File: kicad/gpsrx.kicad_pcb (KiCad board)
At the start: 6 copper layers, 203.2 x 152.4 mm, 284 parts, among them J1 Conn_Coaxial, J10 AVR-JTAG-10, J11 JAE_SIM_Card_SF72S006, J12 Conn_Coaxial, J13 Conn_01x06, J14 Conn_01x06, J2 Conn_Coaxial, J3 Conn_Coaxial, J4 Conn_Coaxial, J5 Conn_Coaxial_Power, J6 Screw_Terminal_01x02, J7 Conn_Coaxial, J8 USB_C_Receptacle_USB2.0_14P, J9 Conn_01x03, Q1 2N7002, SW1 SW_Push, SW2 SW_Push, U1 SIT5156A, U10 AD8350ARZ20-REEL7, U11 ADP7118ACPZN, U12 ESP32-S3-WROOM-1-N8R2, U13 T20Q100F3C3, U14 TMP117xxDRV, U15 OPA376xxDBV, U16 AD5689RxRUZ, U17 JTP32CSV, U18 74AUC1G79, U19 74AUC1G79, U2 5M160ZE64, U20 PE43711B-Z, U21 LTC2386CUH-16-PBF, U22 ADP7118ACPZN, U23 LTM8074EY-PBF, U24 MONARCH_2_GM02S, U25 MCP23S17_SS, U26 TXB0108DQSR, U3 LMK1C1104, U4 LEA-M8T, U5 TDC7200, U6 LMK1C1104, U7 LTM8078EY-PBF, U8 ADP7118ACPZN, U9 ADP7118ACPZN

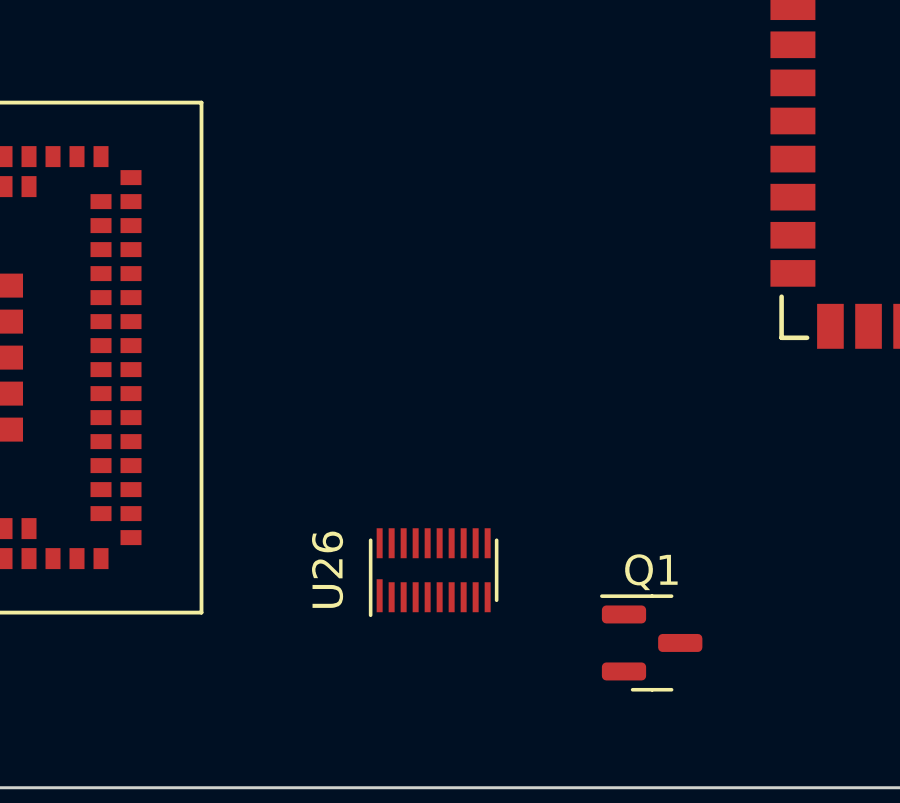
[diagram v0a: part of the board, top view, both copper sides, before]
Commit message: swap txb0108 package, fix pin 65 on cpld
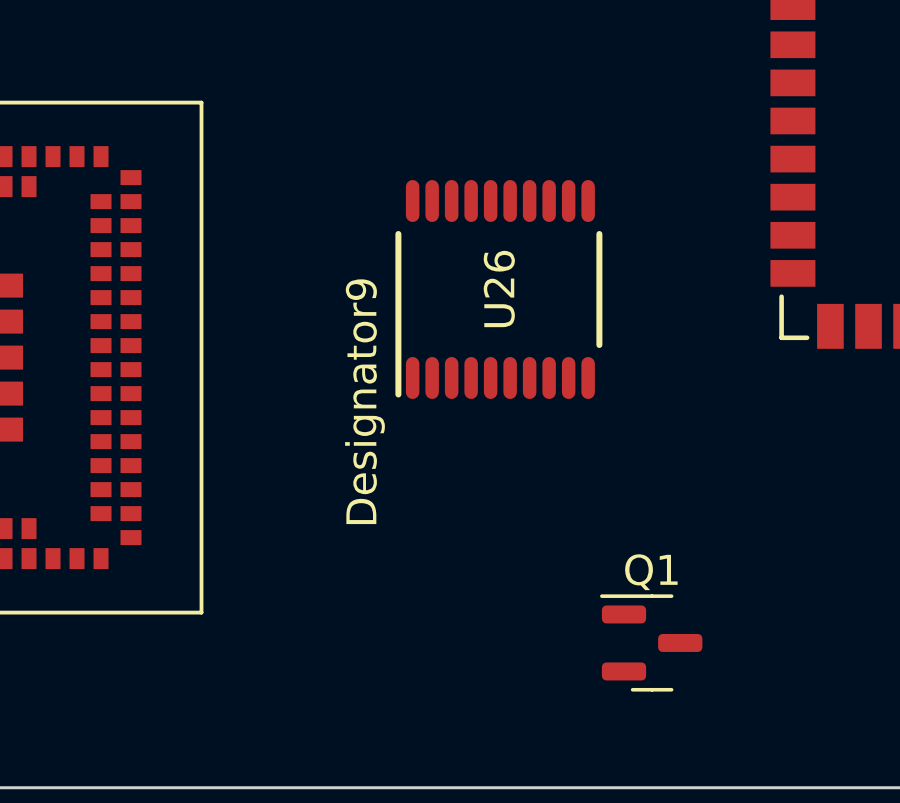
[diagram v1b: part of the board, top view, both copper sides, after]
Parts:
- U26: value TXB0108DQSR -> TXB0108PWR; footprint Package_SON:USON-20_2x4mm_P0.4mm -> bgelb_footprint:PW0020A_N
- moved U26 9.62 mm to (279.8, 190.7)
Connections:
- U26 pad 10: unconnected-(U26-A8-Pad10) -> Net-(U26-OE)
- U26 pad 11: unconnected-(U26-B8-Pad11) -> GND
- U26 pad 14: LTE_TO_UC_CTS -> unconnected-(U26-B6-Pad14)
- U26 pad 15: GND -> LTE_TO_UC_CTS
- U26 pad 16: +3.3V -> UC_TO_LTE_DATA
- U26 pad 17: UC_TO_LTE_DATA -> LTE_TO_UC_DATA
- U26 pad 18: LTE_TO_UC_DATA -> UC_TO_LTE_RTS
- U26 pad 19: UC_TO_LTE_RTS -> +3.3V
- U26 pad 2: /LTE Radio/LTE_RTS0_1V8 -> +3.3V
- U26 pad 3: /LTE Radio/LTE_TXD0_1V8 -> /LTE Radio/LTE_RTS0_1V8
- U26 pad 4: /LTE Radio/LTE_RXD0_1V8 -> /LTE Radio/LTE_TXD0_1V8
- U26 pad 5: +3.3V -> /LTE Radio/LTE_RXD0_1V8
- U26 pad 6: Net-(U26-OE) -> /LTE Radio/LTE_CTS0_1V8
- U26 pad 7: /LTE Radio/LTE_CTS0_1V8 -> unconnected-(U26-A6-Pad7)

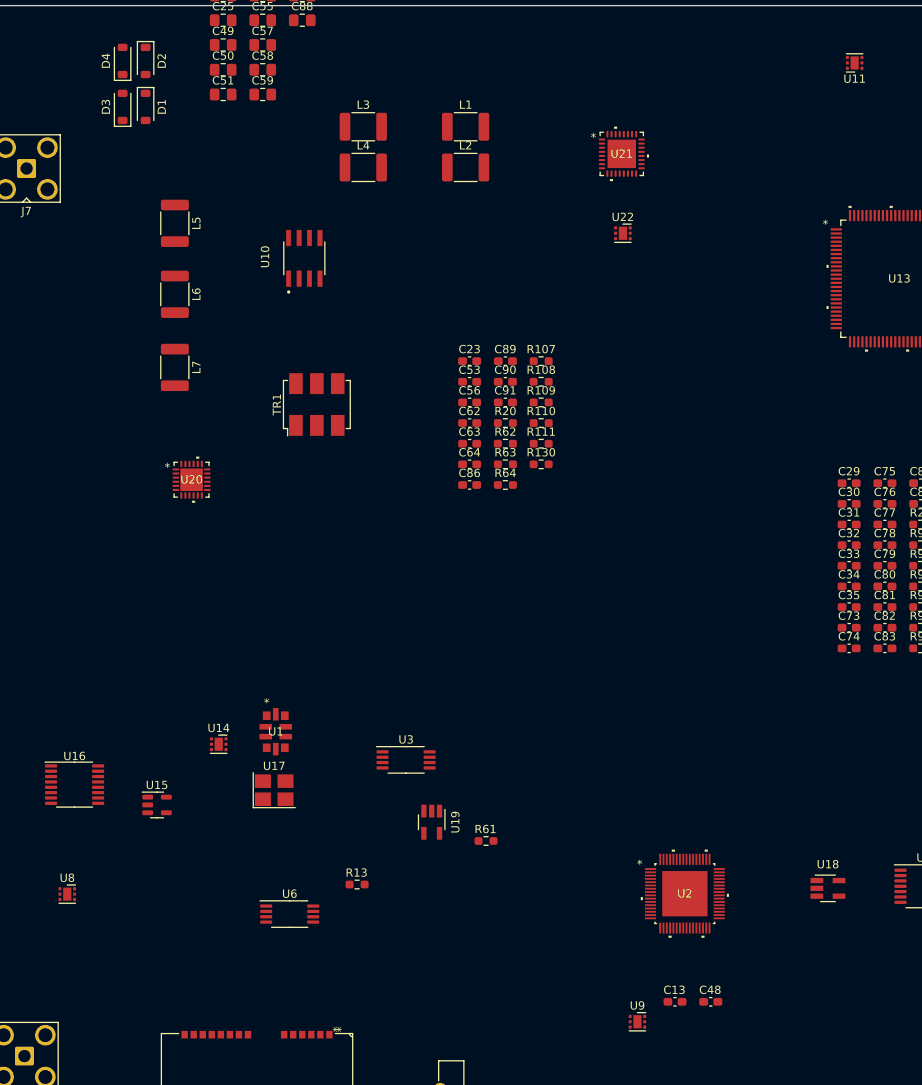
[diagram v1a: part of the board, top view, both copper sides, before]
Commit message: fix adc_clk, adp7118
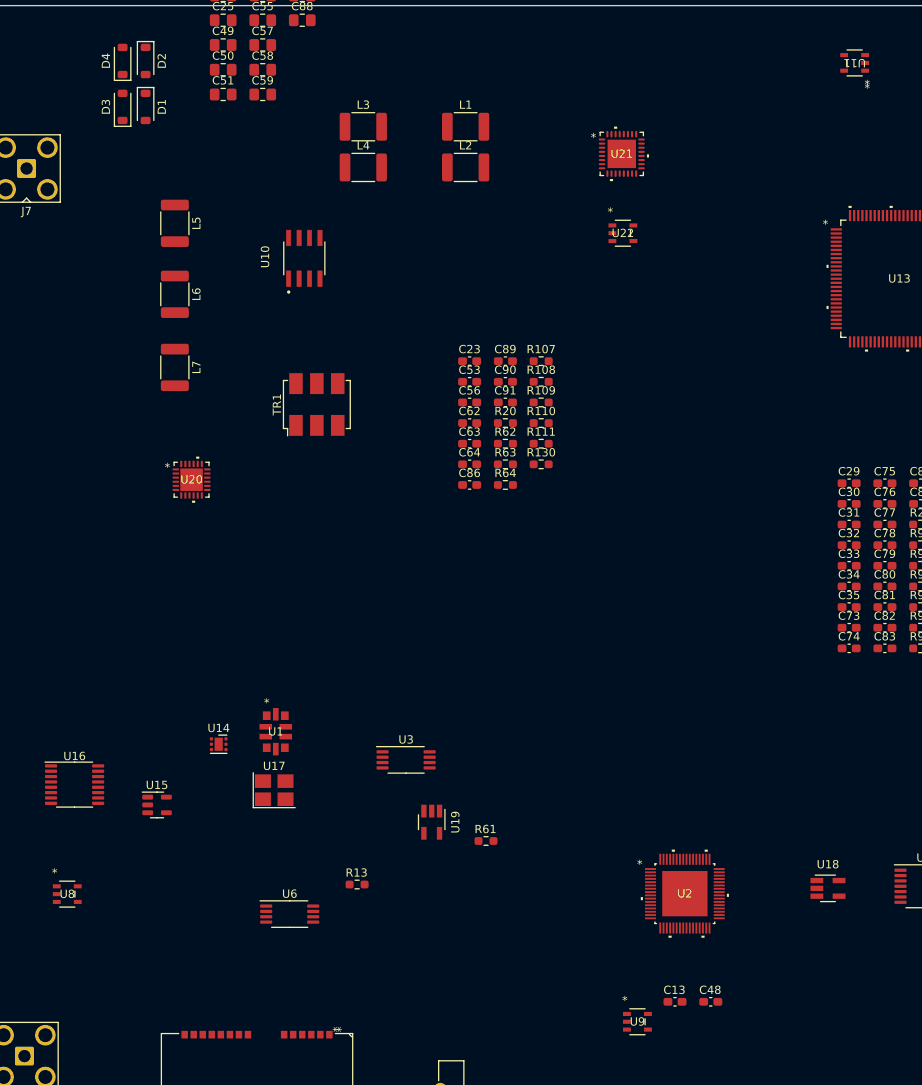
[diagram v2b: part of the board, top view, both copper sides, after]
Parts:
- U11, U22, U8, U9: value ADP7118ACPZN -> ADP7118AUJZ; footprint Package_CSP:LFCSP-6-1EP_2x2mm_P0.65mm_EP1x1.6mm -> bgelb_footprint:UJ_5_ADI
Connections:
- U11 pad 1: +2V5 -> +3.3V
- U11 pad 2: /Power/2V5_SNS -> GND
- U11 pad 3: GND -> /Power/2V5EN
- U11 pad 4: /Power/2V5EN -> /Power/2V5_SNS
- U11 pad 5: unconnected-(U11-SS-Pad5) -> +2V5
- U22 pad 1: +5VA -> /Power/5V5_OUT
- U22 pad 2: /Power/5VA_SNS -> GND
- U22 pad 3: GND -> /Power/5VA_EN
- U22 pad 4: /Power/5VA_EN -> /Power/5VA_SNS
- U22 pad 5: unconnected-(U22-SS-Pad5) -> +5VA
- U8 pad 1: +3.3VA -> /Power/5V5_OUT
- U8 pad 2: /Power/3V3A_SNS -> GND
- U8 pad 3: GND -> /Power/3V3A_EN
- U8 pad 4: /Power/3V3A_EN -> /Power/3V3A_SNS
- U8 pad 5: unconnected-(U8-SS-Pad5) -> +3.3VA
- U9 pad 1: +1V8 -> +3.3V
- U9 pad 2: /Power/1V8_SNS -> GND
- U9 pad 3: GND -> /Power/1V2EN
- U9 pad 4: /Power/1V2EN -> /Power/1V8_SNS
- U9 pad 5: unconnected-(U9-SS-Pad5) -> +1V8

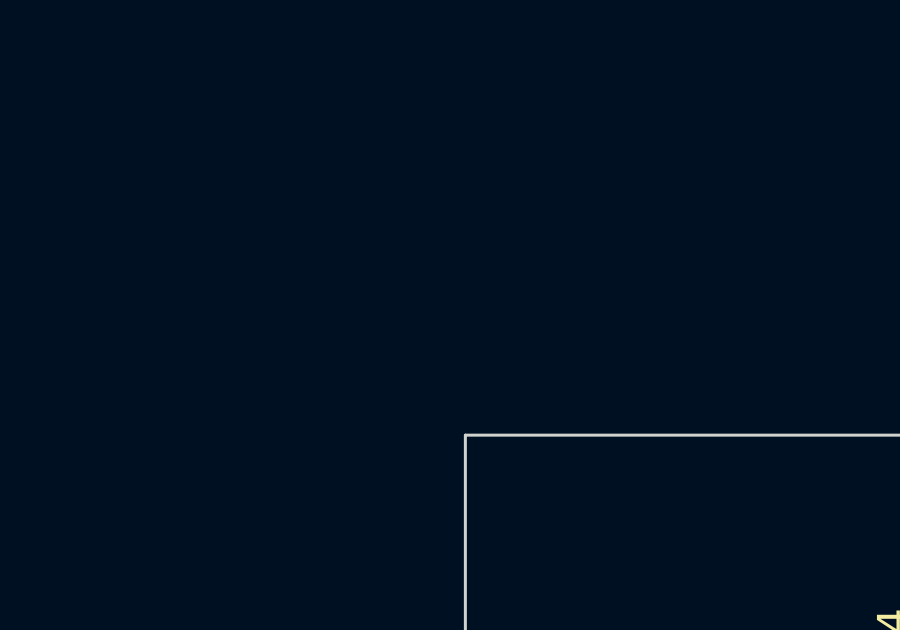
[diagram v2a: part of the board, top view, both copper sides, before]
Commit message: add series term to ioexp_ss_r
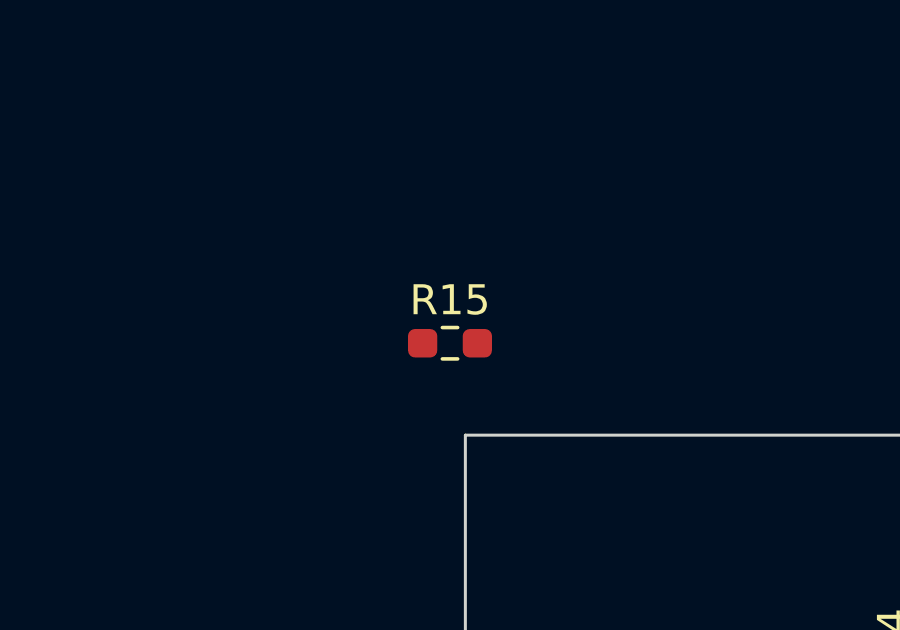
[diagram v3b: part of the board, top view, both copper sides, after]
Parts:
- added R15: 22, Resistor_SMD:R_0603_1608Metric_Pad0.98x0.95mm_HandSolder, F.Cu at (113.8, 51.8)
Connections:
- U12 pad 7: /MCU/SPI_IOEXP_SS -> /MCU/SPI_IOEXP_SS_R
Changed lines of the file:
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@@
   (net 399 "unconnected-(U26-B7-Pad13)")
   (net 400 "unconnected-(U26-B6-Pad14)")
+  (net 401 "/MCU/SPI_IOEXP_SS_R")
   (footprint "Connector_Coaxial:SMA_Amphenol_901-143_Horizontal" (layer "F.Cu")
     (at 310.388 107.092 -90)
@@
       (net 115 "/MCU/SPI_SCK_UC") (pinfunction "IO6") (pintype "bidirectional"))
     (pad "7" smd rect (at -8.75 2.36 270) (size 1.4986 0.889) (layers "F.Cu" "F.Paste" "F.Mask")
-      (net 266 "/MCU/SPI_IOEXP_SS") (pinfunction "IO7") (pintype "bidirectional"))
+      (net 401 "/MCU/SPI_IOEXP_SS_R") (pinfunction "IO7") (pintype "bidirectional"))
     (pad "8" smd rect (at -8.75 3.63 270) (size 1.4986 0.889) (layers "F.Cu" "F.Paste" "F.Mask")
       (net 267 "UC_TO_LTE_RTS") (pinfunction "IO15") (pintype "bidirectional"))
@@
     (model "${KICAD6_3DMODEL_DIR}/Resistor_SMD.3dshapes/R_0603_1608Metric.wrl"
       (offset (xyz 0 0 0))
+      (scale (xyz 1 1 1))
+      (rotate (xyz 0 0 0))
+    )
+  )
+  (footprint "Resistor_SMD:R_0603_1608Metric_Pad0.98x0.95mm_HandSolder" (layer "F.Cu")
+    (at 113.7875 51.8)
+    (descr "Resistor SMD 0603 (1608 Metric), square (rectangular) end terminal, IPC_7351 nominal with elongated pad for handsoldering. (Body size source: IPC-SM-782 page 72, https://www.pcb-3d.com/wordpress/wp-content/uploads/ipc-sm-782a_amendment_1_and_2.pdf), generated with kicad-footprint-generator")
+    (tags "resistor handsolder")
+    (property "Sheetfile" "mcu.kicad_sch")
+    (property "Sheetname" "MCU")
+    (property "ki_description" "Resistor, US symbol")
+    (property "ki_keywords" "R res resistor")
+    (attr smd)
+    (fp_text reference "R15" (at 0 -1.43) (layer "F.SilkS")
+        (effects (font (size 1 1) (thickness 0.15)))
+    )
+    (fp_text value "22" (at 0 1.43) (layer "F.Fab")
+        (effects (font (size 1 1) (thickness 0.15)))
+    )
+    (fp_text user "${REFERENCE}" (at 0 0) (layer "F.Fab")
+        (effects (font (size 0.4 0.4) (thickness 0.06)))
+    )
+    (fp_line (start -0.254724 -0.5225) (end 0.254724 -0.5225)
+      (stroke (width 0.12) (type solid)) (layer "F.SilkS"))
+    (fp_line (start -0.254724 0.5225) (end 0.254724 0.5225)
+      (stroke (width 0.12) (type solid)) (layer "F.SilkS"))
+    (fp_line (start -1.65 -0.73) (end 1.65 -0.73)
+      (stroke (width 0.05) (type solid)) (layer "F.CrtYd"))
+    (fp_line (start -1.65 0.73) (end -1.65 -0.73)
+      (stroke (width 0.05) (type solid)) (layer "F.CrtYd"))
+    (fp_line (start 1.65 -0.73) (end 1.65 0.73)
+      (stroke (width 0.05) (type solid)) (layer "F.CrtYd"))
+    (fp_line (start 1.65 0.73) (end -1.65 0.73)
+      (stroke (width 0.05) (type solid)) (layer "F.CrtYd"))
+    (fp_line (start -0.8 -0.4125) (end 0.8 -0.4125)
+      (stroke (width 0.1) (type solid)) (layer "F.Fab"))
+    (fp_line (start -0.8 0.4125) (end -0.8 -0.4125)
+      (stroke (width 0.1) (type solid)) (layer "F.Fab"))
+    (fp_line (start 0.8 -0.4125) (end 0.8 0.4125)
+      (stroke (width 0.1) (type solid)) (layer "F.Fab"))
+    (fp_line (start 0.8 0.4125) (end -0.8 0.4125)
+      (stroke (width 0.1) (type solid)) (layer "F.Fab"))
+    (pad "1" smd roundrect (at -0.9125 0) (size 0.975 0.95) (layers "F.Cu" "F.Paste" "F.Mask") (roundrect_rratio 0.25)
+      (net 266 "/MCU/SPI_IOEXP_SS") (pintype "passive"))
+    (pad "2" smd roundrect (at 0.9125 0) (size 0.975 0.95) (layers "F.Cu" "F.Paste" "F.Mask") (roundrect_rratio 0.25)
+      (net 401 "/MCU/SPI_IOEXP_SS_R") (pintype "passive"))
+    (model "${KICAD6_3DMODEL_DIR}/Resistor_SMD.3dshapes/R_0603_1608Metric.wrl"
+      (offset (xyz 0 0 0))
